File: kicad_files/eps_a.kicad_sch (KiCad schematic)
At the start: 34 parts, among them J11 5051101592, Q2 TEMT6000X01, U13 MCP3427-xUN, U14 BQ25570

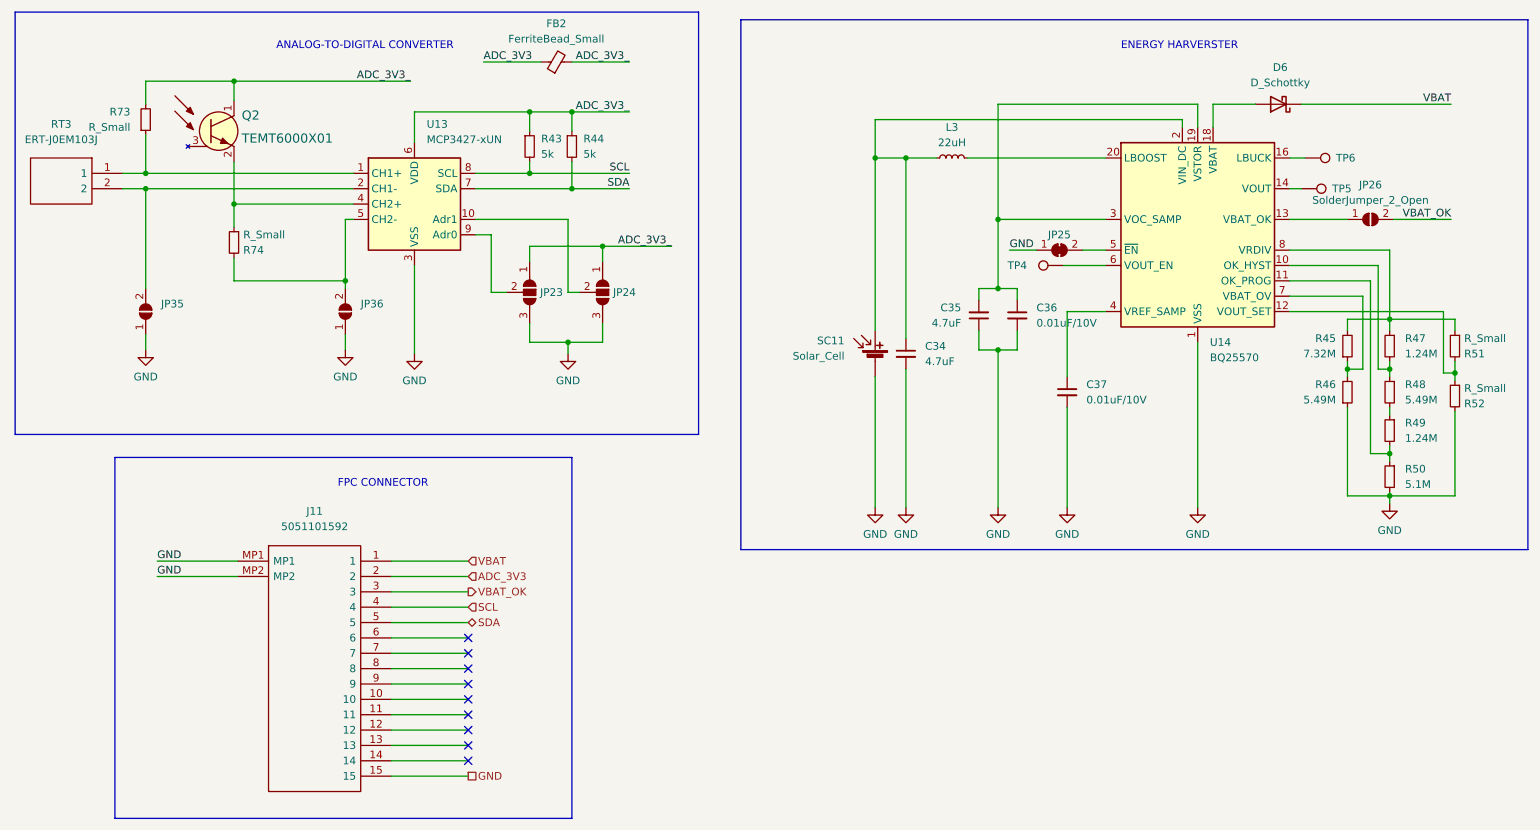
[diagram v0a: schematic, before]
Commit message: update components values
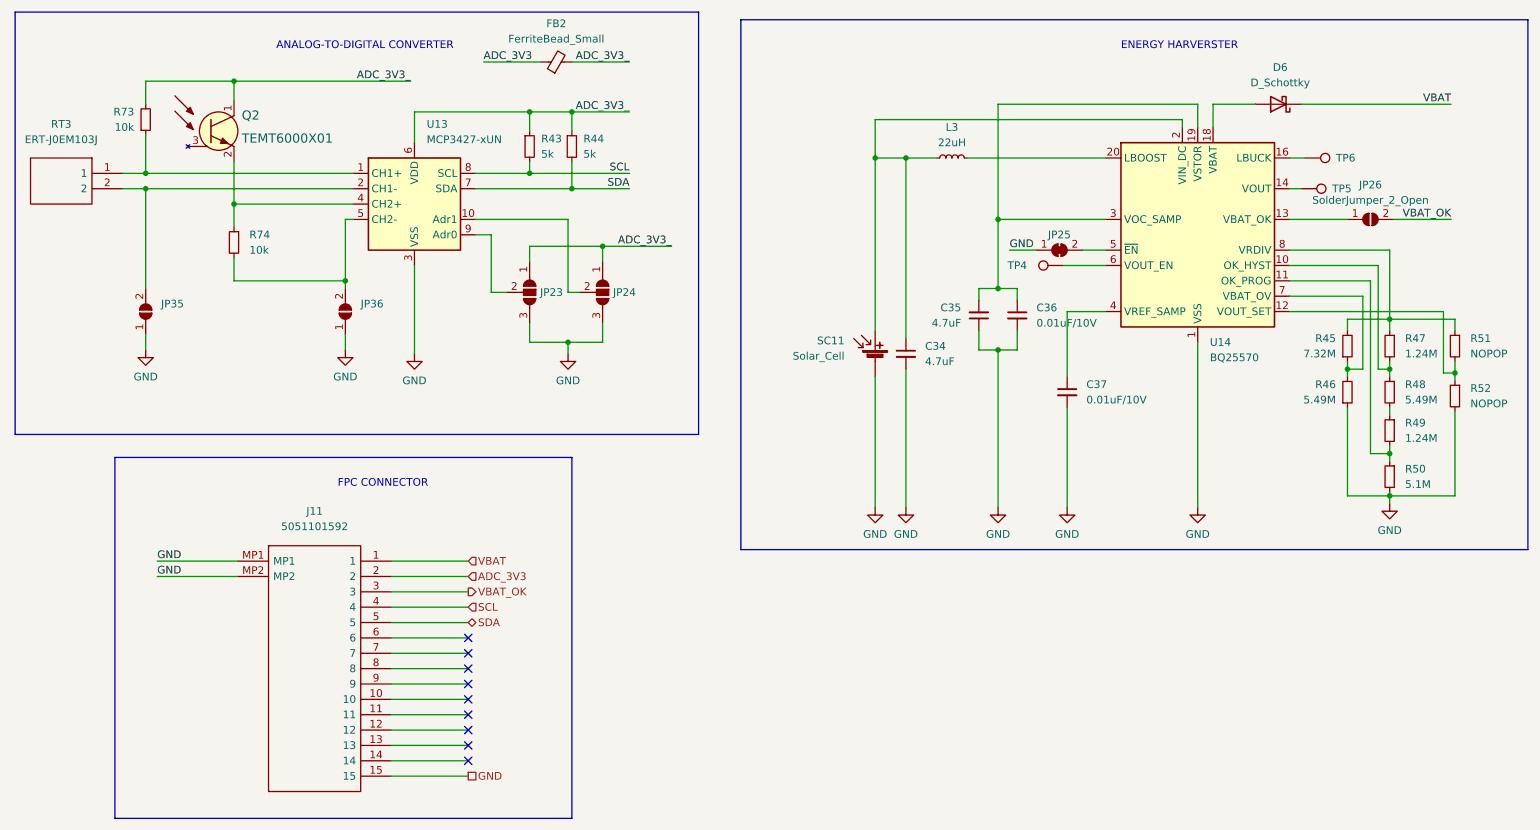
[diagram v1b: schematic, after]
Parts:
- R51, R52: value R_Small -> NOPOP
- R73, R74: value R_Small -> 10k
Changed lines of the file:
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@@
   (symbol (lib_id "Device:R_Small") (at 51.435 48.895 0) (mirror x) (unit 1)
     (in_bom yes) (on_board yes) (fields_autoplaced)
-    (property "Reference" "R73" (id 0) (at 48.895 47.6249 0)
-      (effects (font (size 1.27 1.27)) (justify right))
-    )
-    (property "Value" "R_Small" (id 1) (at 48.895 50.1649 0)
+    (property "Reference" "R73" (id 0) (at 49.53 47.6249 0)
+      (effects (font (size 1.27 1.27)) (justify right))
+    )
+    (property "Value" "10k" (id 1) (at 49.53 50.1649 0)
       (effects (font (size 1.27 1.27)) (justify right))
     )
@@
   (symbol (lib_id "Device:R_Small") (at 267.97 86.36 0) (mirror y) (unit 1)
     (in_bom yes) (on_board yes) (fields_autoplaced)
-    (property "Reference" "R51" (id 0) (at 269.494 87.6301 0)
-      (effects (font (size 1.27 1.27)) (justify right))
-    )
-    (property "Value" "R_Small" (id 1) (at 269.494 85.0901 0)
+    (property "Reference" "R51" (id 0) (at 270.51 85.0899 0)
+      (effects (font (size 1.27 1.27)) (justify right))
+    )
+    (property "Value" "NOPOP" (id 1) (at 270.51 87.6299 0)
       (effects (font (size 1.27 1.27)) (justify right))
     )
@@
   (symbol (lib_id "Device:R_Small") (at 66.04 69.215 0) (mirror y) (unit 1)
     (in_bom yes) (on_board yes) (fields_autoplaced)
-    (property "Reference" "R74" (id 0) (at 67.564 70.4851 0)
-      (effects (font (size 1.27 1.27)) (justify right))
-    )
-    (property "Value" "R_Small" (id 1) (at 67.564 67.9451 0)
+    (property "Reference" "R74" (id 0) (at 68.58 67.9449 0)
+      (effects (font (size 1.27 1.27)) (justify right))
+    )
+    (property "Value" "10k" (id 1) (at 68.58 70.4849 0)
       (effects (font (size 1.27 1.27)) (justify right))
     )
@@
   (symbol (lib_id "Device:R_Small") (at 267.97 94.615 0) (mirror y) (unit 1)
     (in_bom yes) (on_board yes) (fields_autoplaced)
-    (property "Reference" "R52" (id 0) (at 269.494 95.8851 0)
-      (effects (font (size 1.27 1.27)) (justify right))
-    )
-    (property "Value" "R_Small" (id 1) (at 269.494 93.3451 0)
-      (effects (font (size 1.27 1.27)) (justify right))
-    )
+    (property "Reference" "R52" (id 0) (at 270.51 93.3449 0)
+      (effects (font (size 1.27 1.27)) (justify right))
+    )
+    (property "Value" "NOPOP" (id 1) (at 270.51 95.8849 0)
+      (effects (font (size 1.27 1.27)) (justify right))
+    )
